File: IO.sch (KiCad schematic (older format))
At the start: 22 parts, among them SW2 CH1_Vadj, SW3 CH2_Vadj, U5 74HC14, U6 MCP23008-xP, U7 4013

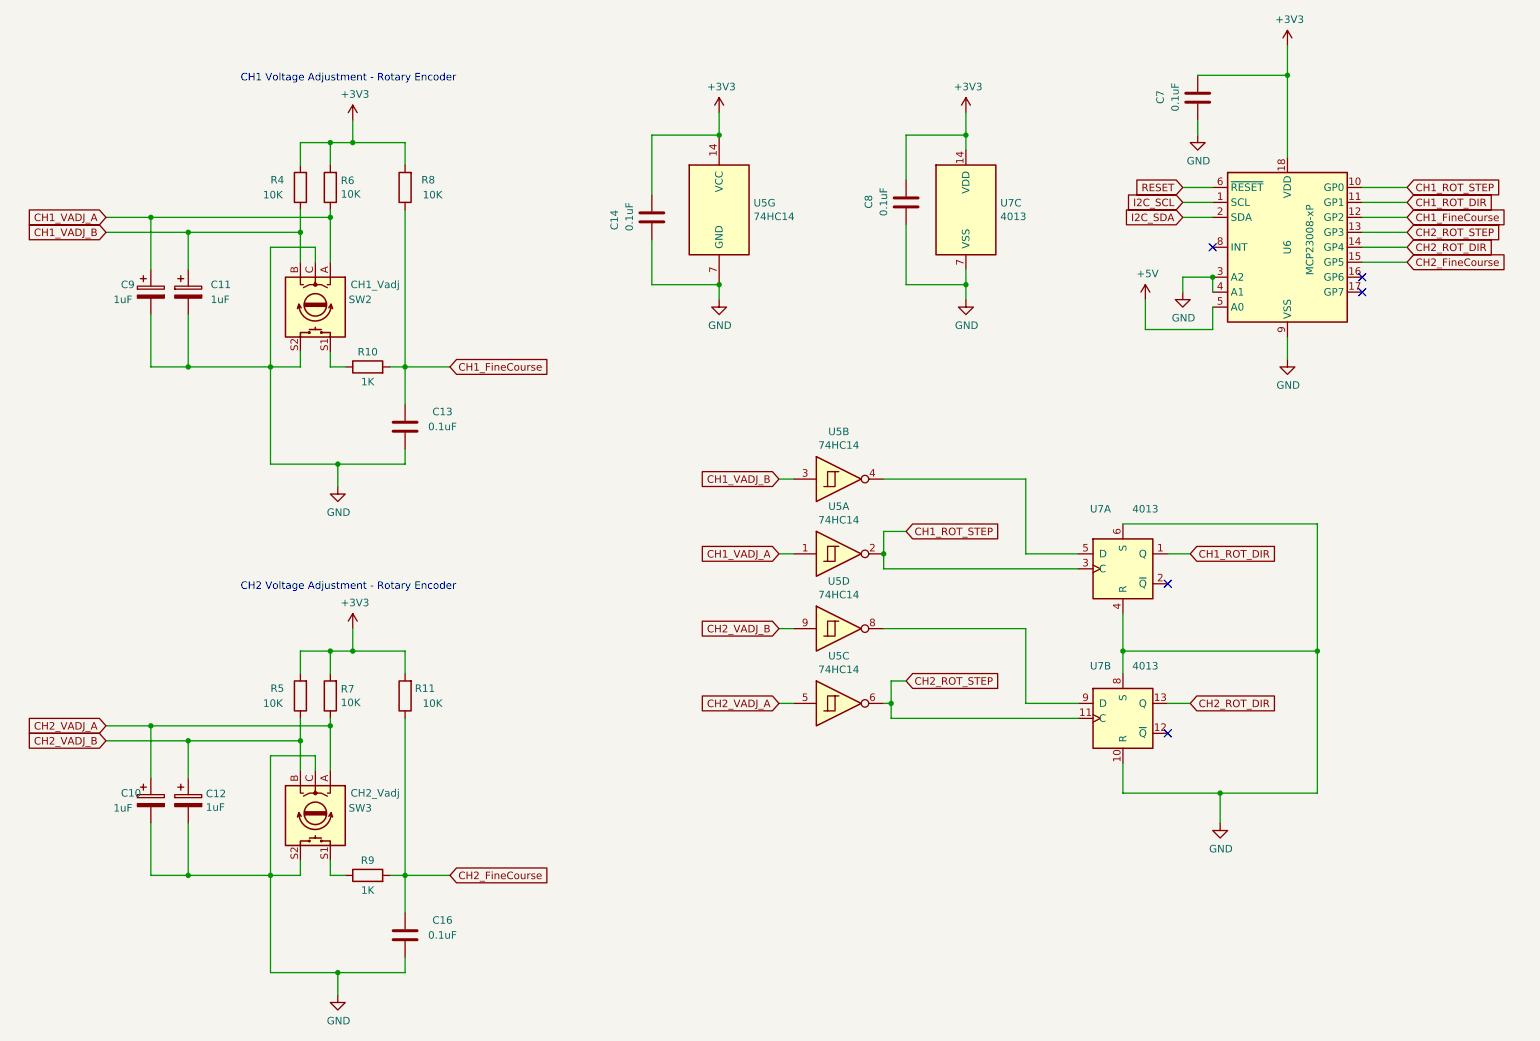
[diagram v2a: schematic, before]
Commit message: We now have more MCU pins. Was able to remove two I2C IO expanders
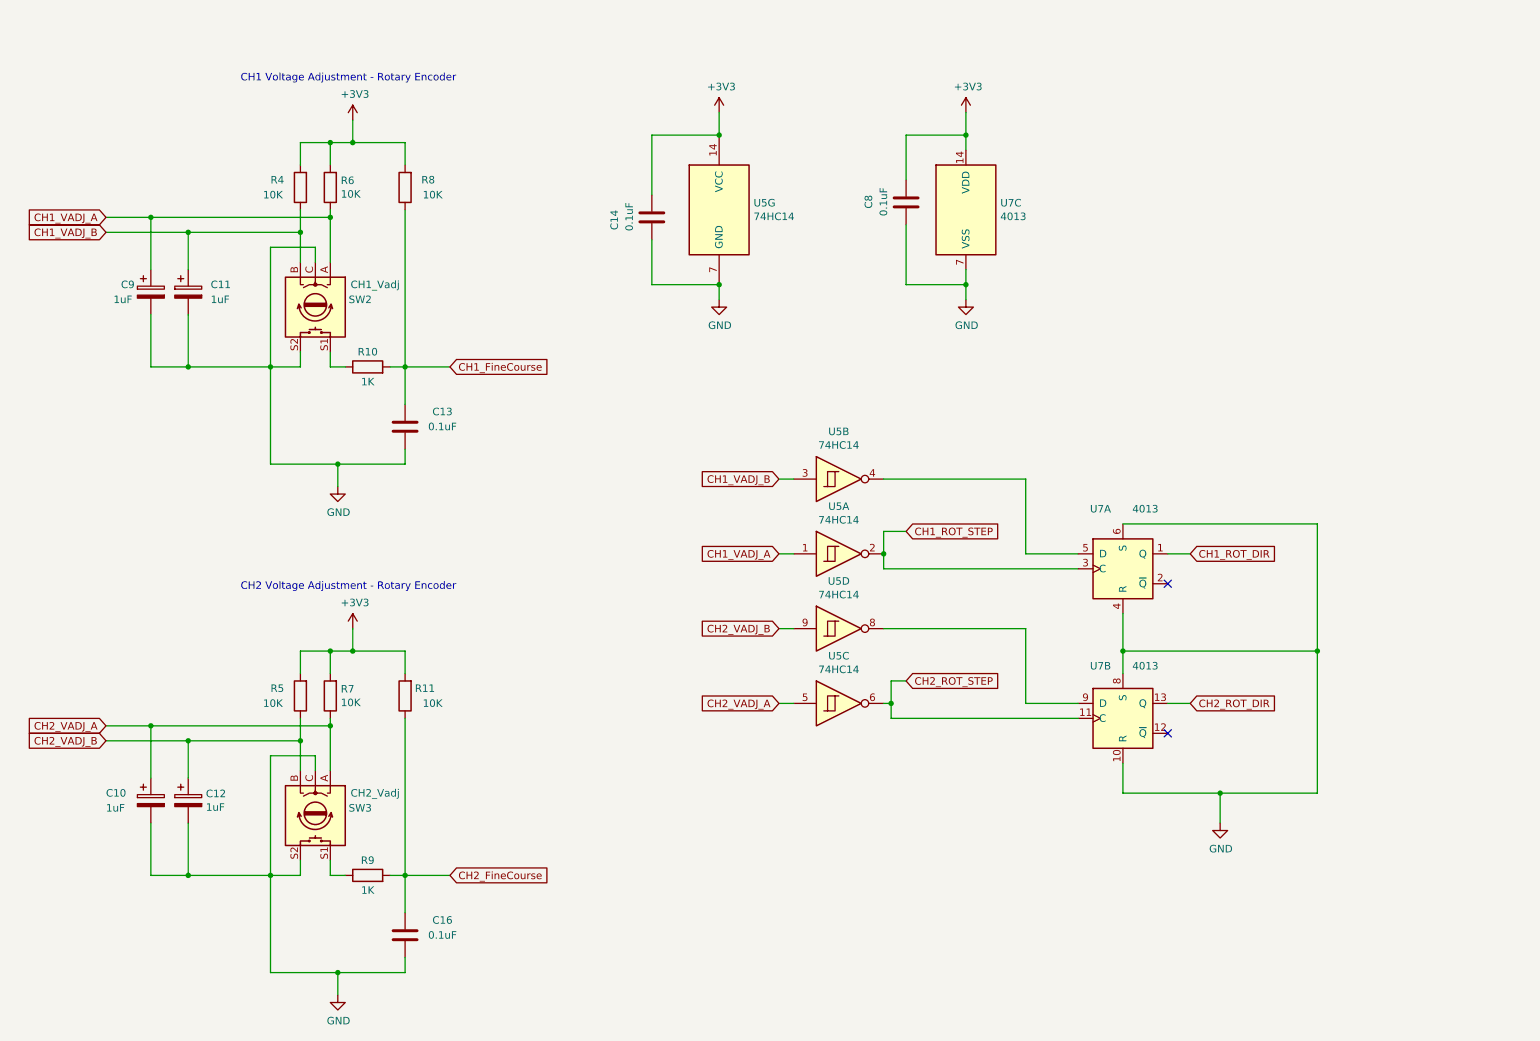
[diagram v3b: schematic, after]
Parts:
- removed C7: 0.1uF, symbol Device:C
- removed U6: MCP23008-xP, Package_DIP:DIP-18_W7.62mm, symbol Interface_Expansion:MCP23008-xP
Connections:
- no-connect marks 5 -> 2
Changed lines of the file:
@@
 $EndDescr
-$Comp
-L Interface_Expansion:MCP23008-xP U?
-U 1 1 605653F1
-P 9250 2250
-AR Path="/605653F1" Ref="U?"  Part="1"
-AR Path="/604E5285/605653F1" Ref="U6"  Part="1"
-F 0 "U6" V 9250 2250 50  0000 C CNN
-F 1 "MCP23008-xP" V 9400 2300 50  0000 C CNN
-F 2 "Package_DIP:DIP-18_W7.62mm" H 9250 1200 50  0001 C CNN
-F 3 "http://ww1.microchip.com/downloads/en/DeviceDoc/MCP23008-MCP23S08-Data-Sheet-20001919F.pdf" H 10550 1050 50  0001 C CNN
-	1    9250 2250
-	1    0    0    -1
-$EndComp
-Wire Wire Line
-	8750 1850 8550 1850
-Wire Wire Line
-	8750 1950 8550 1950
-Wire Wire Line
-	8550 2050 8750 2050
-NoConn ~ 8750 2250
-Wire Wire Line
-	8750 2550 8750 2450
-Wire Wire Line
-	8550 2450 8750 2450
-Connection ~ 8750 2450
-Wire Wire Line
-	8550 2450 8550 2550
-Wire Wire Line
-	8750 2650 8750 2800
-Wire Wire Line
-	8750 2800 8300 2800
-Wire Wire Line
-	8300 2800 8300 2600
-$Comp
-L power:+5V #PWR?
-U 1 1 60565405
-P 8300 2600
-AR Path="/60565405" Ref="#PWR?"  Part="1"
-AR Path="/604E5285/60565405" Ref="#PWR0115"  Part="1"
-F 0 "#PWR0115" H 8300 2450 50  0001 C CNN
-F 1 "+5V" H 8315 2773 50  0000 C CNN
-F 2 "" H 8300 2600 50  0001 C CNN
-F 3 "" H 8300 2600 50  0001 C CNN
-	1    8300 2600
-	1    0    0    -1
-$EndComp
-$Comp
-L power:GND #PWR?
-U 1 1 6056540B
-P 8550 2550
-AR Path="/6056540B" Ref="#PWR?"  Part="1"
-AR Path="/604E5285/6056540B" Ref="#PWR0116"  Part="1"
-F 0 "#PWR0116" H 8550 2300 50  0001 C CNN
-F 1 "GND" H 8555 2377 50  0000 C CNN
-F 2 "" H 8550 2550 50  0001 C CNN
-F 3 "" H 8550 2550 50  0001 C CNN
-	1    8550 2550
-	1    0    0    -1
-$EndComp
-Wire Wire Line
-	9250 2850 9250 3000
-$Comp
-L power:GND #PWR?
-U 1 1 60565412
-P 9250 3000
-AR Path="/60565412" Ref="#PWR?"  Part="1"
-AR Path="/604E5285/60565412" Ref="#PWR0117"  Part="1"
-F 0 "#PWR0117" H 9250 2750 50  0001 C CNN
-F 1 "GND" H 9255 2827 50  0000 C CNN
-F 2 "" H 9250 3000 50  0001 C CNN
-F 3 "" H 9250 3000 50  0001 C CNN
-	1    9250 3000
-	1    0    0    -1
-$EndComp
-$Comp
-L Device:C C?
-U 1 1 60565418
-P 8650 1250
-AR Path="/60565418" Ref="C?"  Part="1"
-AR Path="/604E5285/60565418" Ref="C7"  Part="1"
-F 0 "C7" V 8900 1200 50  0000 L CNN
-F 1 "0.1uF" V 8800 1150 50  0000 L CNN
-F 2 "" H 8688 1100 50  0001 C CNN
-F 3 "~" H 8650 1250 50  0001 C CNN
-	1    8650 1250
-	-1   0    0    1
-$EndComp
-$Comp
-L power:GND #PWR?
-U 1 1 6056541E
-P 8650 1500
-AR Path="/6056541E" Ref="#PWR?"  Part="1"
-AR Path="/604E5285/6056541E" Ref="#PWR0118"  Part="1"
-F 0 "#PWR0118" H 8650 1250 50  0001 C CNN
-F 1 "GND" H 8655 1327 50  0000 C CNN
-F 2 "" H 8650 1500 50  0001 C CNN
-F 3 "" H 8650 1500 50  0001 C CNN
-	1    8650 1500
-	1    0    0    -1
-$EndComp
-Wire Wire Line
-	8650 1400 8650 1500
-Wire Wire Line
-	8650 1100 9250 1100
-Wire Wire Line
-	9250 1100 9250 1650
-Wire Wire Line
-	9250 1100 9250 900
-Connection ~ 9250 1100
-Wire Wire Line
-	9750 1850 10050 1850
-Wire Wire Line
-	9750 1950 10050 1950
-Wire Wire Line
-	9750 2050 10050 2050
-Wire Wire Line
-	9750 2150 10050 2150
-Wire Wire Line
-	9750 2250 10050 2250
-Wire Wire Line
-	9750 2350 10050 2350
 $Comp
 L Device:R R?
@@
 U 1 1 6076B16D
 P 1650 5950
-F 0 "C10" H 1450 6000 50  0000 L CNN
-F 1 "1uF" H 1400 5900 50  0000 L CNN
+F 0 "C10" H 1350 6000 50  0000 L CNN
+F 1 "1uF" H 1350 5900 50  0000 L CNN
 F 2 "" H 1688 5800 50  0001 C CNN
 F 3 "~" H 1650 5950 50  0001 C CNN
@@
 Wire Wire Line
 	6550 4150 6700 4150
-Text GLabel 10050 1850 2    50   Input ~ 0
-CH1_ROT_STEP
-Text GLabel 10050 2150 2    50   Input ~ 0
-CH2_ROT_STEP
-Text GLabel 10050 1950 2    50   Input ~ 0
-CH1_ROT_DIR
-Text GLabel 10050 2250 2    50   Input ~ 0
-CH2_ROT_DIR
-Text GLabel 10050 2050 2    50   Input ~ 0
-CH1_FineCourse
-Text GLabel 10050 2350 2    50   Input ~ 0
-CH2_FineCourse
-NoConn ~ 9750 2450
-NoConn ~ 9750 2550
-Text GLabel 8550 1950 0    50   Input ~ 0
-I2C_SCL
-Text GLabel 8550 2050 0    50   Input ~ 0
-I2C_SDA
-Text GLabel 8550 1850 0    50   Input ~ 0
-RESET
 $Comp
 L power:+3V3 #PWR?
@@
 	1    0    0    -1
 $EndComp
-$Comp
-L power:+3V3 #PWR?
-U 1 1 600CB0A8
-P 9250 900
-F 0 "#PWR?" H 9250 750 50  0001 C CNN
-F 1 "+3V3" H 9265 1073 50  0000 C CNN
-F 2 "" H 9250 900 50  0001 C CNN
-F 3 "" H 9250 900 50  0001 C CNN
-	1    9250 900
-	1    0    0    -1
-$EndComp
